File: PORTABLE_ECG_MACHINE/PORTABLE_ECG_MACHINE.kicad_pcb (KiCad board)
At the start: 2 copper layers, 25.5 x 64.8 mm, 89 parts, among them IC1 AD8232ACPZ, J1 UART, J2 ECG PROBE, J3 Li-Ion 3.7 CONN, J4 USB_C_Receptacle_USB2.0, J5 Conn_01x06_Male, Q1 BSS138, Q2 BSS138, SW1 SW_SPDT, U2 CP2102-GM, U3 ATmega328PB-A, U4 LM3940IMP-3.3/NOPB, U5 TP4056, U6 SSD1306, Y1 16MHZ

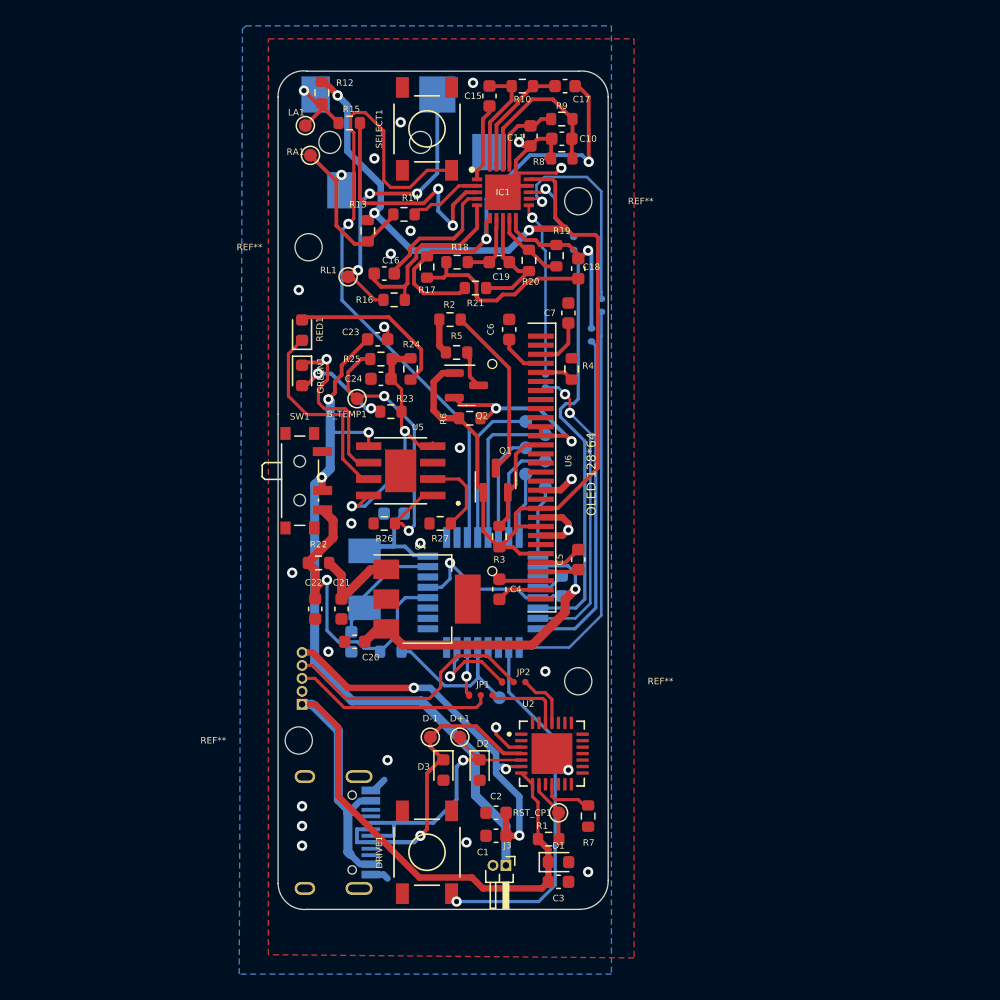
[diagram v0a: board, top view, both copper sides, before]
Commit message: schematics update
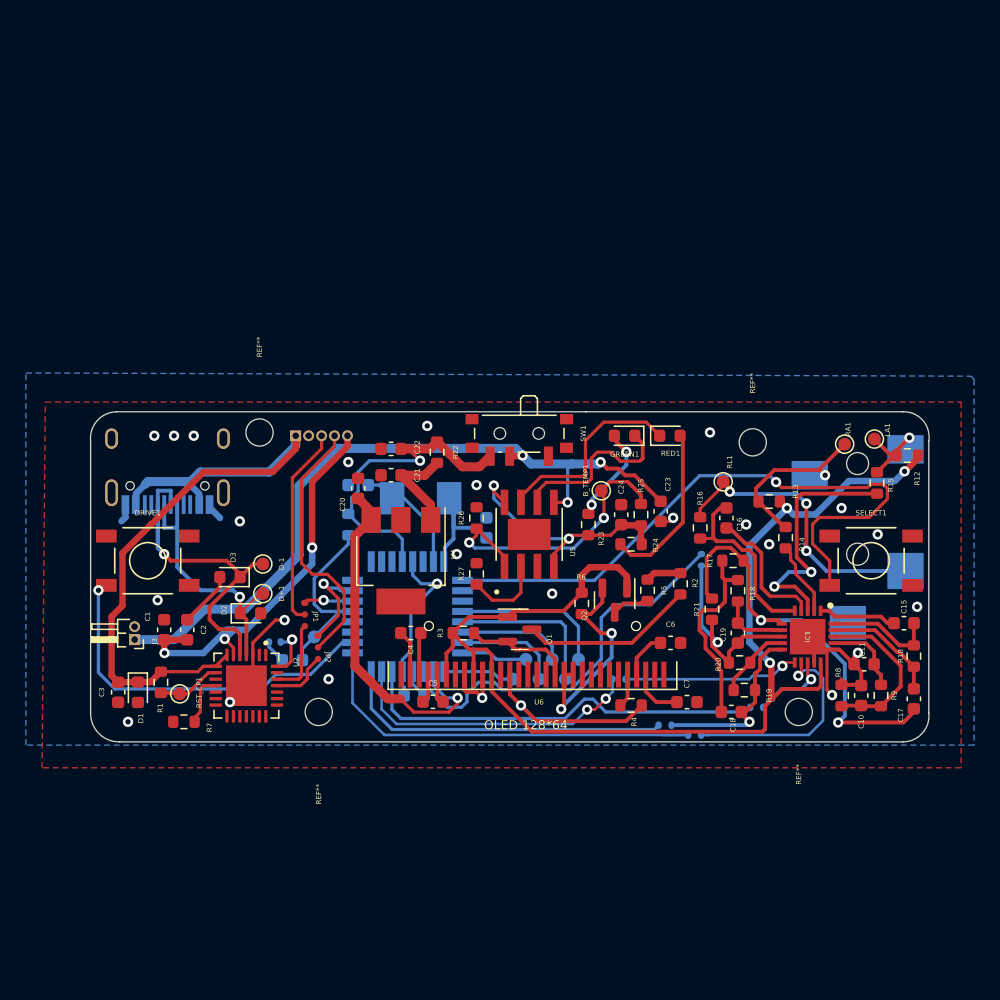
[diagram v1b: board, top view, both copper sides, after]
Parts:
- added C8: .1uf, Capacitor_SMD:C_0603_1608Metric, B.Cu at (85.1, 70.0)
- added JP7: REF, TEST_POINT_MATRIX_6-PIN:2_PIN_SMD_SOLDER_JUMPER, B.Cu at (112.9, 61.1)
- added JP8: RST, TEST_POINT_MATRIX_6-PIN:2_PIN_SMD_SOLDER_JUMPER, B.Cu at (82.6, 72.4)
- R14, R15: value 10M -> 180k
- R16: value 10M -> 360k
- moved C17 54.5 mm to (133.1, 73.0), turned to 90 degrees
- moved R10 53.4 mm to (133.1, 69.7), turned to 90 degrees
- moved R12 53.2 mm to (132.6, 54.2), turned to 180 degrees
- moved C15 51.8 mm to (132.4, 67.1), turned to 0 degrees
- moved R9 50.9 mm to (130.6, 72.7), turned to -90 degrees
- moved LA1 50.2 mm to (130.1, 52.9), turned to -90 degrees
- moved R15 49.4 mm to (130.3, 56.3), turned to -90 degrees
- moved C10 48.8 mm to (129.0, 72.7), turned to -90 degrees
- moved C11 48.3 mm to (129.3, 70.3), turned to 0 degrees
- moved SELECT1 47.9 mm to (129.8, 62.3), turned to 0 degrees
- moved J2 47.0 mm to (128.8, 57.3), turned to 180 degrees
- moved RA1 46.9 mm to (127.8, 53.3), turned to -90 degrees
- moved R8 46.8 mm to (127.5, 72.7), turned to -90 degrees
- moved REF** 43.0 mm to (124.2, 74.0), turned to -90 degrees
- moved IC1 41.6 mm to (124.9, 68.2), turned to -90 degrees
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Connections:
- net Net-(C12-Pad2) renamed /REF_IN
- C24 pad 2: unconnected-(C24-Pad2) -> GND
- U2 pad 28: unconnected-(U2-Pad28) -> Net-(U2-Pad28)
- U2 pad 4: /USB_D- -> /USB_D+
- U2 pad 5: /USB_D+ -> /USB_D-
- U3 pad 11: Net-(SELECT1-Pad3) -> unconnected-(U3-Pad11)
- U3 pad 9: unconnected-(U3-Pad9) -> Net-(SELECT1-Pad3)
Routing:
- net /REF_IN: track 2.21 -> 32.0 mm
- net GND: track 43.1 -> 60.9 mm
- net /REF_OUT: track 9.19 -> 16.2 mm, vias 0 -> 1
- net Net-(U2-Pad28): track 0.00 -> 3.93 mm, vias 0 -> 1
- net +3V3: track 24.0 -> 27.3 mm
- net Net-(C8-Pad1): track 0.00 -> 1.82 mm
- net /SDA_3.3: track 15.3 -> 16.9 mm
- net /RST#: track 14.2 -> 15.5 mm
- net Net-(C5-Pad2): track 3.32 -> 2.42 mm
- net Net-(SELECT1-Pad3): track 50.2 -> 49.5 mm
- net Net-(C5-Pad1): track 2.96 -> 2.27 mm
- net /AT_SDN#: track 32.7 -> 32.1 mm
- net Net-(GREEN1-Pad1): track 13.4 -> 13.5 mm, vias 1 -> 0
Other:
- board size 25.5 x 64.8 mm -> 64.8 x 25.5 mm

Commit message: rev3 fab files, board pdf
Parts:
- moved C24 2.30 mm to (109.9, 61.0), turned to -90 degrees
- moved R24 1.25 mm to (112.4, 61.6)
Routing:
- net GND: track 60.9 -> 67.1 mm
- net Net-(C24-Pad1): track 19.9 -> 21.0 mm
- net Net-(GREEN1-Pad2): track 6.83 -> 7.70 mm
- net Net-(B_TEMP1-Pad1): track 23.3 -> 23.9 mm
